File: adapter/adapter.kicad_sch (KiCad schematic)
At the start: 8 parts, among them U1 TPS61041DBV

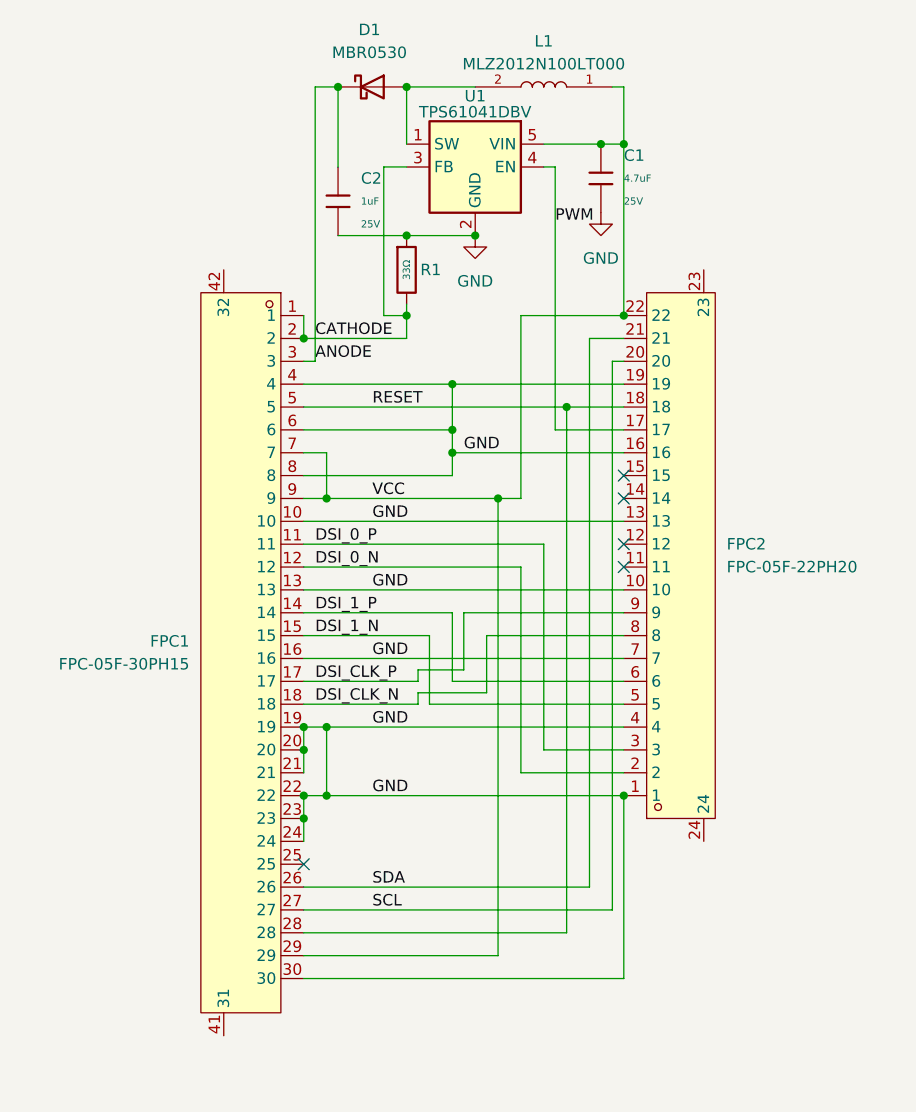
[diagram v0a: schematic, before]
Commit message: fix a few messed up traces, pass DRU
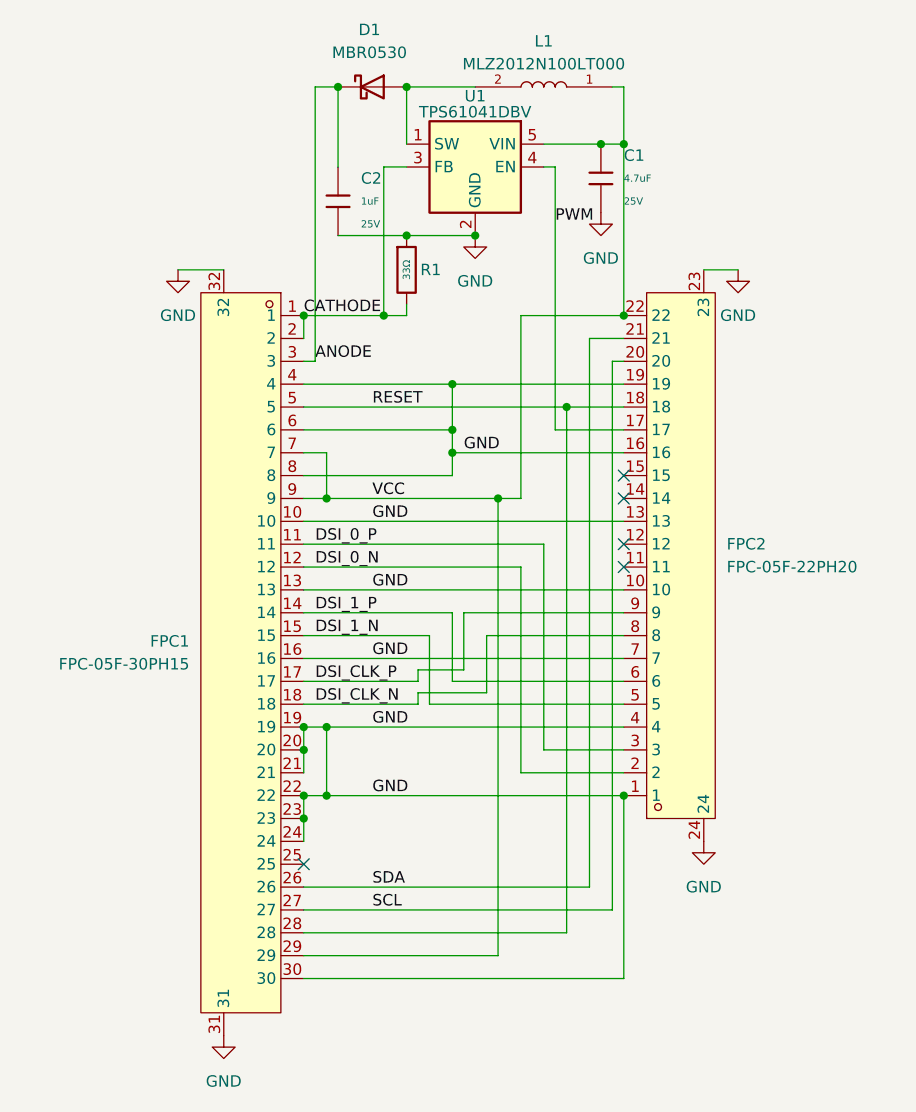
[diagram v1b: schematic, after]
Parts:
- D1: LCSC Part (none) -> C77336
- L1: LCSC Part (none) -> C1046
- U1: LCSC Part (none) -> C5145241
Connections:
- net ANODE: no longer FPC1.1, FPC1.2, R1.2, U1.3 (FB)
- net GND: now also FPC1.31, FPC1.32, FPC2.23, FPC2.24
- new net CATHODE: FPC1.1, FPC1.2, R1.2, U1.3 (FB)
